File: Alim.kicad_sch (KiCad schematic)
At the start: 48 parts, among them J7 +12V, J8 +12V, U1 OPA1612, U2 OPA1644, U3 PCM3060, U4 NE5532, U5 PGA2310, U6 LM317_SOT-223, U7 LM337_SOT223, U8 L78L05_SOT89

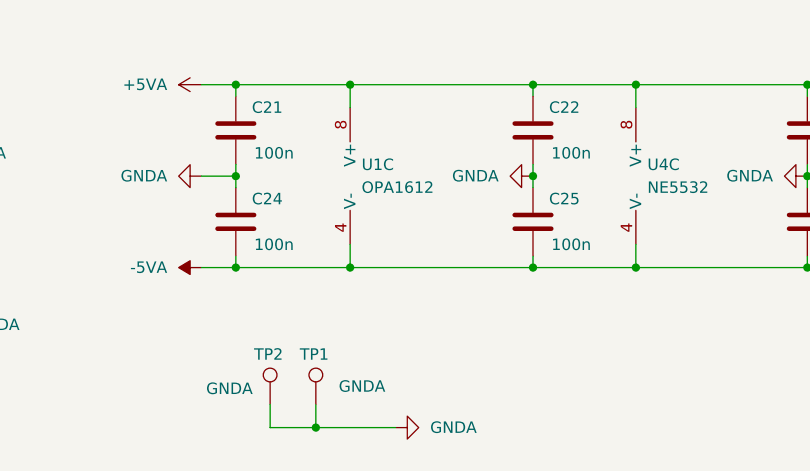
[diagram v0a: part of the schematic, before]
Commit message: Fix typo OPA1612 -> OPA1642. Note: an OPA with FET inputs is necessary here.
/!\  An OPA with FET inputs is necessary here.
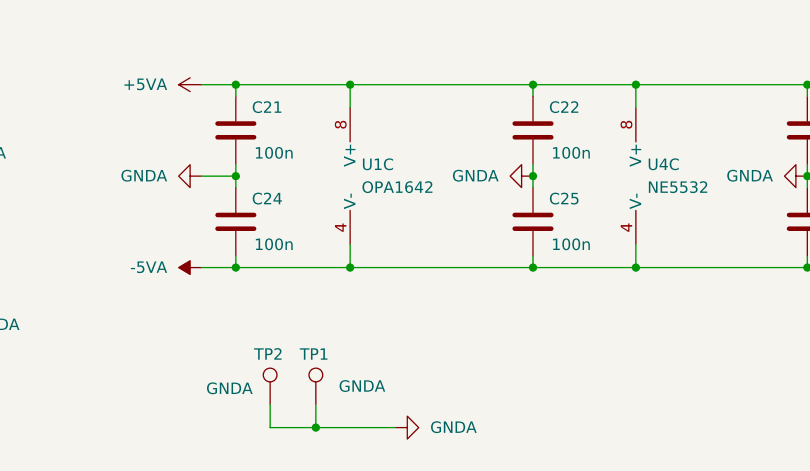
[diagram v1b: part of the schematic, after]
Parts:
- U1: value OPA1612 -> OPA1642
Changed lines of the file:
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@@
 			)
 		)
-		(property "Value" "OPA1612"
+		(property "Value" "OPA1642"
 			(at 195.58 39.3699 0)
 			(effects

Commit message: Invert output summing stage to maintain correct phase
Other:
- note added: "Option 1M and 100n or R0"
- title: OSCAR Audio 1.0 -> OSCAR Audio 01 V2
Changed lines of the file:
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@@
 	(paper "A4")
 	(title_block
-		(title "OSCAR Audio 1.0")
+		(title "OSCAR Audio 01 V2")
 		(date "2025-05-30")
-		(rev "2")
+		(rev "2.1")
 		(company "DAD Design")
 	)
+	(rectangle
+		(start 107.95 83.82)
+		(end 152.4 121.92)
+		(stroke
+			(width 0)
+			(type default)
+		)
+		(fill
+			(type none)
+		)
+	)
+	(text "Option\n1M and 100n\nor\nR0"
+		(exclude_from_sim no)
+		(at 141.224 90.932 0)
+		(effects
+			(font
+				(size 1.524 1.524)
+			)
+		)
+	)
 	(junction
